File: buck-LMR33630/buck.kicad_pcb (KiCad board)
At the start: 2 copper layers, 93 x 67 mm, 22 parts, among them J1 USB-C Connector, P1 BATT-P, P2 BATT-N, P3 5V, SW1 RST, U1 LMR33630ADDA

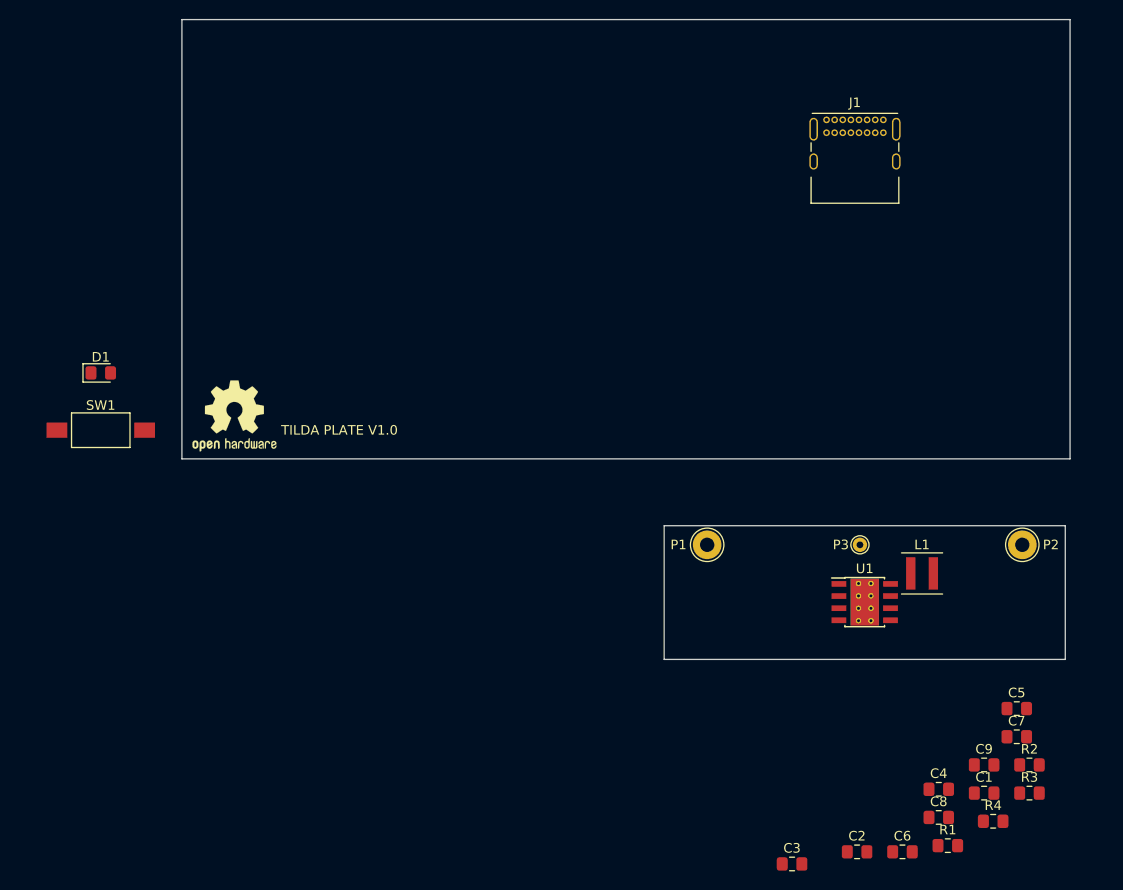
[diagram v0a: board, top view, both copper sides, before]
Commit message: routed buck converter and added usb type c connector
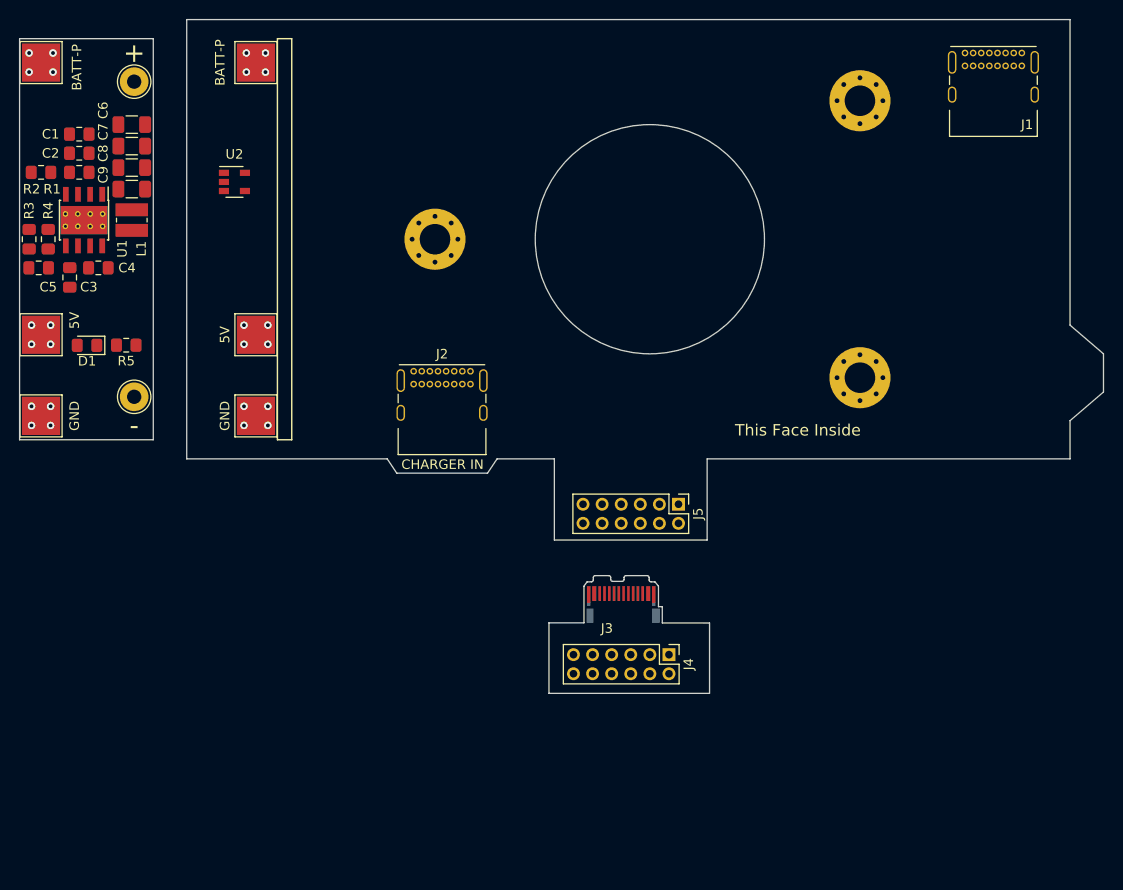
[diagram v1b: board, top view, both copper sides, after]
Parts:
- removed SW1: RST, Button_Switch_SMD:SW_SPST_FSMSM
- added H1: MountingHole 1, MountingHole:MountingHole_3.2mm_M3_Pad_Via, F.Cu at (123.5, 37.0)
- added H2: MountingHole 1, MountingHole:MountingHole_3.2mm_M3_Pad_Via, F.Cu at (168.0, 51.5)
- added H3: MountingHole 1, MountingHole:MountingHole_3.2mm_M3_Pad_Via, F.Cu at (168.0, 22.5)
- added J2: USB-C Connector, Connector_USB:USB_C_Receptacle_GCT_USB4085, F.Cu at (121.3, 50.8)
- added J3: USB_C_Receptacle, Connector_USB:USB_C_Plug_JAE_DX07P024AJ1, F.Cu at (143.0, 75.2)
- added J4: Conn_02x06_Odd_Even, Connector_PinHeader_2.00mm:PinHeader_2x06_P2.00mm_Vertical, F.Cu at (148.0, 80.5)
- added J5: Conn_02x06_Odd_Even, Connector_PinHeader_2.00mm:PinHeader_2x06_P2.00mm_Vertical, F.Cu at (149.0, 64.8)
- added P4: 5V, TestPoint:TestPoint_Pad_4.0x4.0mm, F.Cu at (104.8, 55.5)
- added P5: Pad BATT.P, TestPoint:TestPoint_Pad_4.0x4.0mm, F.Cu at (82.2, 18.5)
- added P6: Pad 5V, TestPoint:TestPoint_Pad_4.0x4.0mm, F.Cu at (82.2, 47.0)
- added P7: Pad GND, TestPoint:TestPoint_Pad_4.0x4.0mm, F.Cu at (82.2, 55.5)
- added P8: BATT-P, TestPoint:TestPoint_Pad_4.0x4.0mm, F.Cu at (104.8, 18.5)
- added R5: 100k, Resistor_SMD:R_0805_2012Metric_Pad1.15x1.40mm_HandSolder, F.Cu at (91.2, 48.1)
- added U2: LMR62421XMF, Package_TO_SOT_SMD:SOT-23-5, F.Cu at (102.5, 31.0)
- C6, C7, C8, C9: footprint Capacitor_SMD:C_0805_2012Metric_Pad1.15x1.40mm_HandSolder -> Capacitor_SMD:C_1206_3216Metric
- L1: value 1.2uH -> 1.5uH; footprint Inductor_SMD:L_Coilcraft_XxL4020 -> Inductor_SMD:L_Wuerth_MAPI-3020
- P3: value 5V -> GND; footprint TestPoint:TestPoint_THTPad_D1.5mm_Drill0.7mm -> TestPoint:TestPoint_Pad_4.0x4.0mm
- logo1: footprint Symbol:OSHW-Logo2_9.8x8mm_SilkScreen -> Symbol:OSHW-Symbol_6.7x6mm_SilkScreen; moved to B.Cu
- moved R2 120.7 mm to (82.2, 30.0)
- moved R3 119.7 mm to (81.0, 37.0), turned to 90 degrees
- moved C1 117.2 mm to (86.2, 26.0), turned to 180 degrees
- moved R4 116.2 mm to (83.0, 37.0), turned to 270 degrees
- moved R1 115.1 mm to (86.2, 30.0)
- moved C5 112.3 mm to (82.0, 40.0)
- moved C7 111.4 mm to (91.8, 27.2), turned to 180 degrees
- moved C6 111.0 mm to (91.8, 25.0), turned to 180 degrees
- moved C2 109.5 mm to (86.2, 28.0), turned to 180 degrees
- moved C8 108.5 mm to (91.8, 29.5), turned to 180 degrees
- moved C9 107.7 mm to (91.8, 31.8), turned to 180 degrees
- moved C4 103.6 mm to (88.2, 40.0)
- moved C3 97.4 mm to (85.2, 41.0), turned to 270 degrees
- moved P2 94.3 mm to (92.0, 53.5), turned to 270 degrees
- moved U1 91.0 mm to (86.8, 35.0), turned to 270 degrees
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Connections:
- net /BATT-P renamed /BATT.P
- C5 pad 1: Net-(C5-Pad1) -> /5V
- C6 pad 1: Net-(C5-Pad1) -> /5V
- C7 pad 1: Net-(C5-Pad1) -> /5V
- C8 pad 1: Net-(C5-Pad1) -> /5V
- C9 pad 1: Net-(C5-Pad1) -> /5V
- D1 pad 2: Net-(D1-Pad2) -> /5V
- J1 pad S1: Net-(J1-PadS1) -> Net-(J1-PadA1)
- L1 pad 1: Net-(C5-Pad1) -> /5V
- P3 pad 1: Net-(C5-Pad1) -> Net-(P3-Pad1)
- R3 pad 2: Net-(C5-Pad1) -> /5V
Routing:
- net Net-(P8-Pad1): vias 0 -> 4
- net Net-(P4-Pad1): vias 0 -> 4
- net Net-(P3-Pad1): vias 0 -> 4
- net GND: vias 0 -> 4
- net /BATT.P: vias 0 -> 4
- net /5V: vias 0 -> 4
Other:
- board size 93 x 67 mm -> 113.5 x 70.6 mm
- board text added: "+"
- board text added: "-"
- board text added: "5V"
- board text added: "BATT-P"
- board text added: "CHARGER IN"
- board text added: "GND"
- board text added: "TILTA PLATE V1.0"
- board text added: "This Face Inside"
- board text removed: "TILDA PLATE V1.0"

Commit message: added lithium c2S charger and tried to route USB3... quite difficult
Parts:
- added L2: 10uH, Inductor_SMD:L_Wuerth_MAPI-4030, F.Cu at (109.0, 78.5)
- added U3: LT3650EDD-8.2TRPBF, Package_SO:MSOP-12-1EP_3x4mm_P0.65mm_EP1.65x2.85mm_ThermalVias, F.Cu at (115.0, 78.5)
- H2: value MountingHole 1 -> MountingHole 2
- H3: value MountingHole 1 -> MountingHole 3
- J4, J5: value Conn_02x06_Odd_Even -> Conn_02x08_Odd_Even; footprint Connector_PinHeader_2.00mm:PinHeader_2x06_P2.00mm_Vertical -> Connector_PinHeader_2.00mm:PinHeader_2x08_P2.00mm_Vertical
- moved U2 47.5 mm to (101.5, 78.5)
- moved J4 3.04 mm to (151.0, 80.0)
- moved J5 2.02 mm to (151.0, 64.5)
- moved J3 1.00 mm to (144.0, 75.2)
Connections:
- net Net-(P4-Pad1) renamed /BATT_5V
- H1 pad 1: (no net) -> GNDA
- H2 pad 1: (no net) -> GNDA
- H3 pad 1: (no net) -> GNDA
- J2 pad A1: Net-(J2-PadA1) -> GNDA
- J2 pad A12: Net-(J2-PadA1) -> GNDA
- J2 pad B1: Net-(J2-PadA1) -> GNDA
- J2 pad B12: Net-(J2-PadA1) -> GNDA
- J2 pad S1: Net-(J2-PadS1) -> GNDA
- J4 pad 11: Net-(J3-PadA1) -> Net-(J4-Pad11)
- J4 pad 2: Net-(J4-Pad2) -> Net-(J3-PadA4)
- J4 pad 3: Net-(J3-PadA7) -> Net-(J4-Pad3)
- J4 pad 5: Net-(J3-PadA6) -> Net-(J4-Pad5)
- J4 pad 7: Net-(J4-Pad7) -> Net-(J3-PadA7)
- J4 pad 9: Net-(J4-Pad9) -> Net-(J3-PadA6)
- J5 pad 1: Net-(J5-Pad1) -> GNDA
- P3 pad 1: Net-(P3-Pad1) -> GNDA
- U2 pad 5: Net-(U2-Pad5) -> Net-(J2-PadA4)
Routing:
- net Net-(J3-PadA7): track 0.00 -> 11.1 mm, vias 0 -> 1
- net Net-(J3-PadA6): track 0.00 -> 11.1 mm, vias 0 -> 1
- net Net-(J3-PadA4): track 0.00 -> 2.00 mm
- net Net-(P3-Pad1): vias 4 -> 0
- net GNDA: vias 0 -> 4
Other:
- board size 113.5 x 70.6 mm -> 113.5 x 70.5 mm
